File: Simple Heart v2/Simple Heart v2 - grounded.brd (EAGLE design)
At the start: 70 x 50 mm, 22 parts

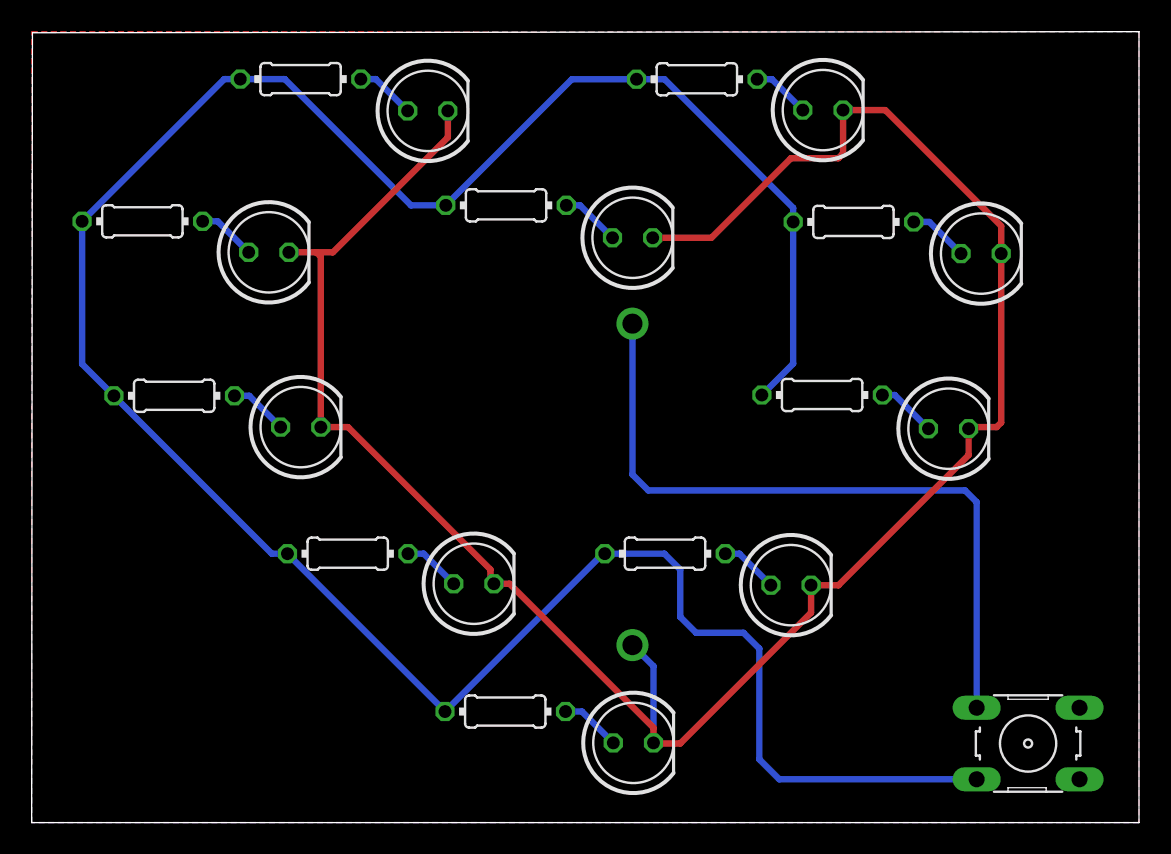
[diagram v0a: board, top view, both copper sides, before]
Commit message: Moving switch location a bit, added oshpark image. Need to confirm text.
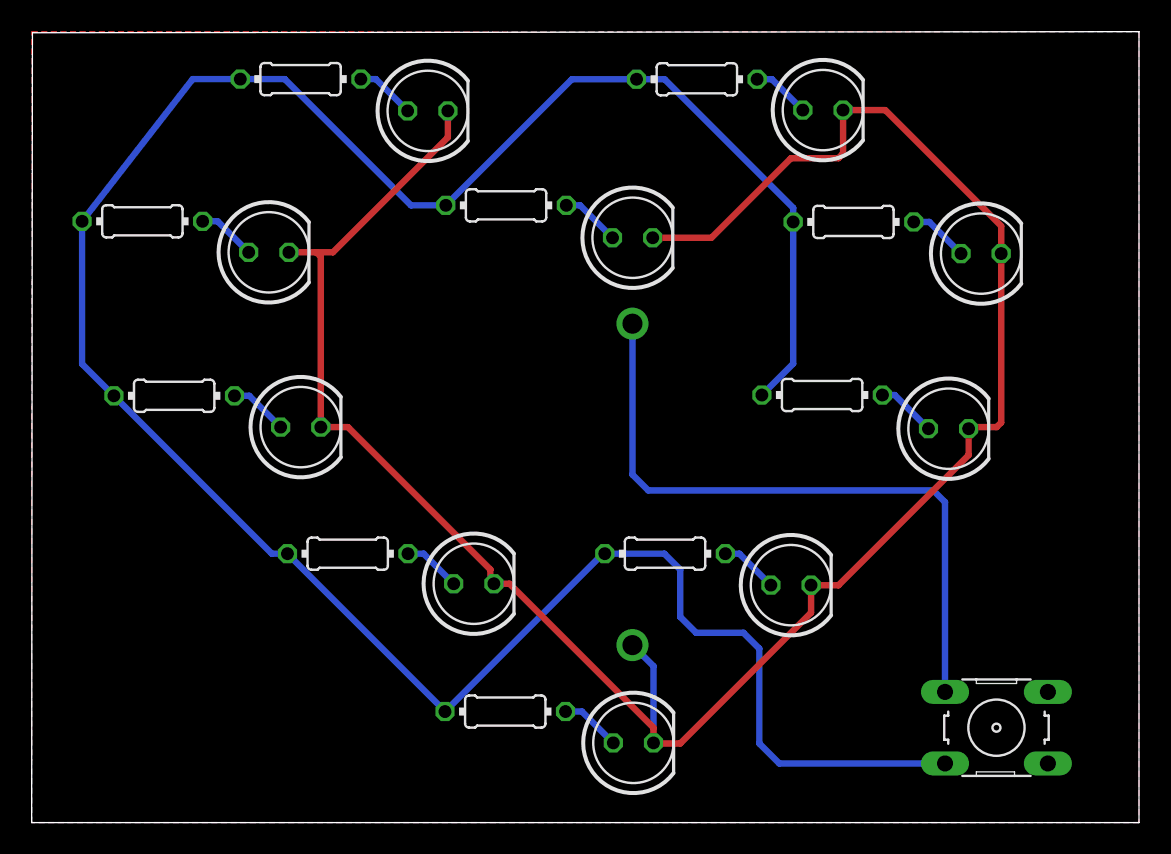
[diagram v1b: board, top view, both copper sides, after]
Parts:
- moved S1 2.24 mm to (61.0, 6.00)
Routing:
- net N$11: track 45.0 -> 42.0 mm
- net N$12: track 161.9 -> 159.6 mm
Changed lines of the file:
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@@
 <attribute name="VALUE" x="38.4144" y="16.5174" size="0.9906" layer="27" ratio="10"/>
 </element>
-<element name="S1" library="switch-omron" package="B3F-10XX" value="" x="62.99" y="5" smashed="yes">
-<attribute name="MPN" value="B3F-1000" x="62.99" y="5" size="1.778" layer="27" display="off"/>
-<attribute name="OC_NEWARK" value="36M3542" x="62.99" y="5" size="1.778" layer="27" display="off"/>
-<attribute name="OC_FARNELL" value="176432" x="62.99" y="5" size="1.778" layer="27" display="off"/>
-<attribute name="MF" value="" x="62.99" y="5" size="1.778" layer="27" display="off"/>
-<attribute name="NAME" x="62.942" y="9.683" size="1.27" layer="26" ratio="10" rot="MR0"/>
-<attribute name="VALUE" x="59.942" y="-0.08" size="1.27" layer="27" ratio="10"/>
+<element name="S1" library="switch-omron" package="B3F-10XX" value="" x="60.99" y="6" smashed="yes">
+<attribute name="MPN" value="B3F-1000" x="60.99" y="6" size="1.778" layer="27" display="off"/>
+<attribute name="OC_NEWARK" value="36M3542" x="60.99" y="6" size="1.778" layer="27" display="off"/>
+<attribute name="OC_FARNELL" value="176432" x="60.99" y="6" size="1.778" layer="27" display="off"/>
+<attribute name="MF" value="" x="60.99" y="6" size="1.778" layer="27" display="off"/>
+<attribute name="NAME" x="60.942" y="10.683" size="1.27" layer="26" ratio="10" rot="MR0"/>
+<attribute name="VALUE" x="57.942" y="0.92" size="1.27" layer="27" ratio="10"/>
 </element>
 </elements>
@@
 <wire x1="5.2" y1="26.98" x2="3.19" y2="28.99" width="0.4064" layer="16"/>
 <wire x1="3.19" y1="28.99" x2="3.19" y2="38.01" width="0.4064" layer="16"/>
-<wire x1="3.19" y1="38.01" x2="12.18" y2="47" width="0.4064" layer="16"/>
-<wire x1="12.18" y1="47" x2="13.19" y2="47" width="0.4064" layer="16"/>
+<wire x1="3.19" y1="38.01" x2="10.18" y2="47" width="0.4064" layer="16"/>
+<wire x1="10.18" y1="47" x2="13.19" y2="47" width="0.4064" layer="16"/>
 <wire x1="36.23" y1="17" x2="36.11" y2="17" width="0.4064" layer="16"/>
 <wire x1="36.11" y1="17" x2="26.13" y2="7.02" width="0.4064" layer="16"/>
@@
 <wire x1="40.01" y1="46.99" x2="48.14" y2="38.86" width="0.4064" layer="16"/>
 <wire x1="48.14" y1="37.97" x2="48.14" y2="38.86" width="0.4064" layer="16"/>
-<wire x1="59.7388" y1="2.7394" x2="47.2606" y2="2.7394" width="0.4064" layer="16"/>
-<wire x1="47.2606" y1="2.7394" x2="46" y2="4" width="0.4064" layer="16"/>
-<wire x1="46" y1="4" x2="46" y2="11" width="0.4064" layer="16"/>
+<wire x1="57.7388" y1="3.7394" x2="47.2606" y2="3.7394" width="0.4064" layer="16"/>
+<wire x1="47.2606" y1="3.7394" x2="46" y2="5" width="0.4064" layer="16"/>
+<wire x1="46" y1="5" x2="46" y2="11" width="0.4064" layer="16"/>
 <wire x1="46" y1="11" x2="45" y2="12" width="0.4064" layer="16"/>
 <wire x1="45" y1="12" x2="42" y2="12" width="0.4064" layer="16"/>
@@
 <contactref element="BATTERY_1" pad="+"/>
 <contactref element="S1" pad="1"/>
-<wire x1="59.7388" y1="7.2606" x2="59.7388" y2="20.2612" width="0.4064" layer="16"/>
+<wire x1="57.7388" y1="8.2606" x2="57.7388" y2="20.2612" width="0.4064" layer="16"/>
 <wire x1="37.98" y1="31.54" x2="37.98" y2="22" width="0.4064" layer="16"/>
-<wire x1="59.7388" y1="20.2612" x2="59" y2="21" width="0.4064" layer="16"/>
-<wire x1="59" y1="21" x2="38.98" y2="21" width="0.4064" layer="16"/>
+<wire x1="57.7388" y1="20.2612" x2="57" y2="21" width="0.4064" layer="16"/>
+<wire x1="57" y1="21" x2="38.98" y2="21" width="0.4064" layer="16"/>
 <wire x1="38.98" y1="21" x2="37.98" y2="22" width="0.4064" layer="16"/>
 </signal>

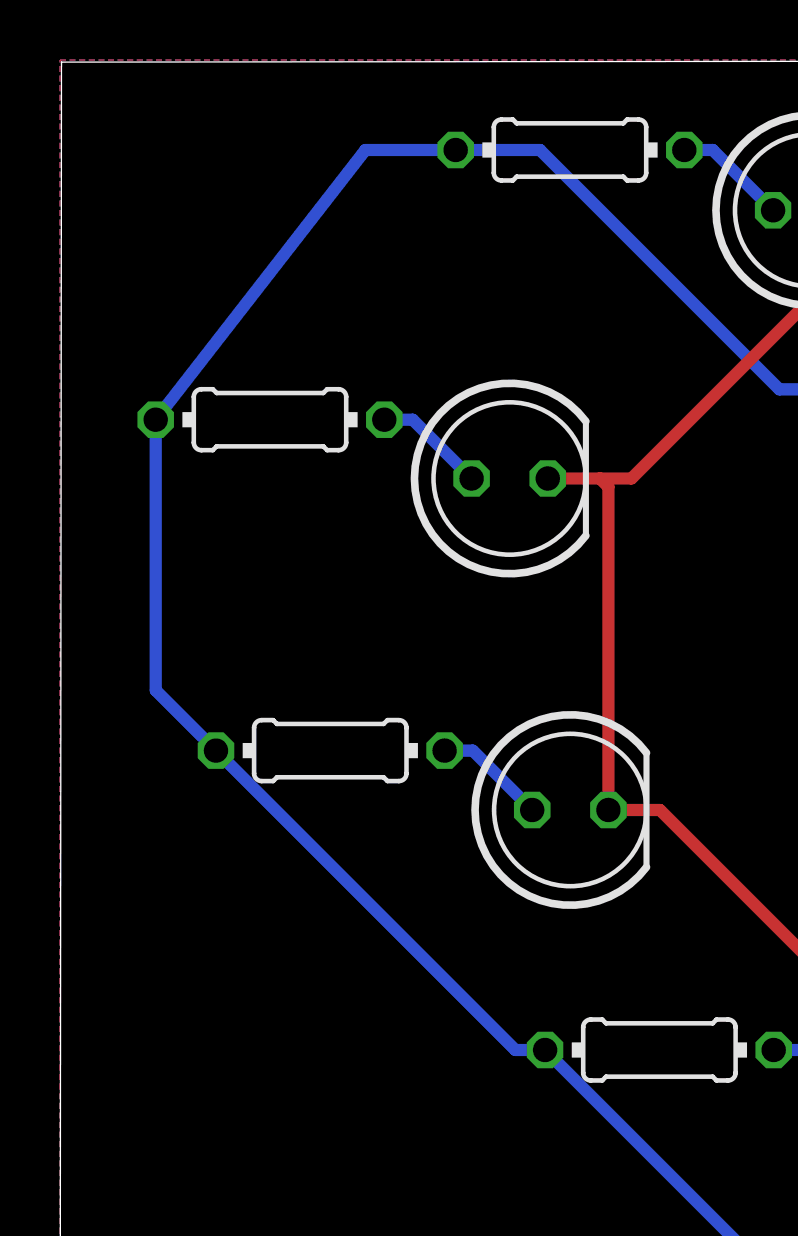
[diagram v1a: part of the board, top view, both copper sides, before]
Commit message: OCDing on the power line routing...it's not symetrical yet. But closer.
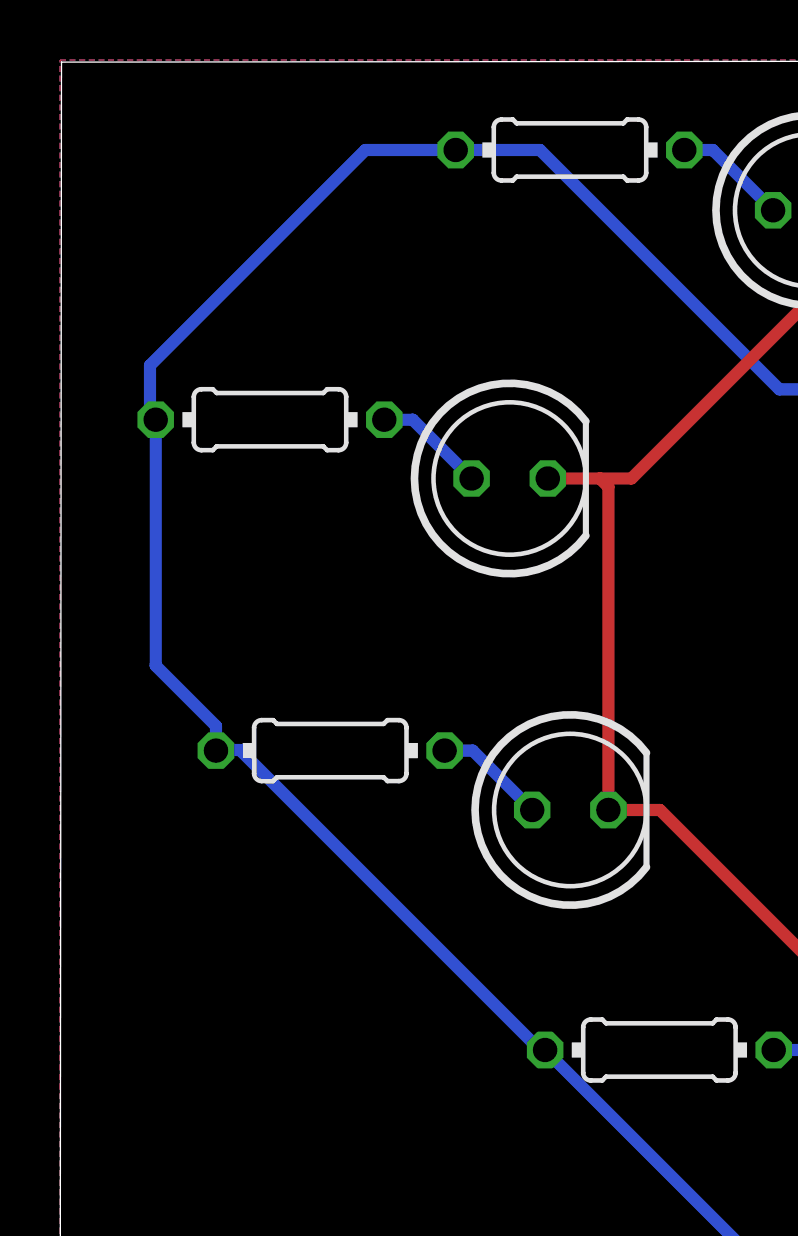
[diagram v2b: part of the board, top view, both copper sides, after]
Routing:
- net N$12: track 159.6 -> 160.2 mm
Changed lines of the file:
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@@
 <contactref element="R10" pad="1"/>
 <contactref element="S1" pad="3"/>
-<wire x1="26.13" y1="7.02" x2="26.13" y2="7.04" width="0.4064" layer="16"/>
-<wire x1="26.13" y1="7.04" x2="16.17" y2="17" width="0.4064" layer="16"/>
-<wire x1="16.17" y1="17" x2="15.18" y2="17" width="0.4064" layer="16"/>
-<wire x1="15.18" y1="17" x2="5.2" y2="26.98" width="0.4064" layer="16"/>
-<wire x1="5.2" y1="26.98" x2="3.19" y2="28.99" width="0.4064" layer="16"/>
-<wire x1="3.19" y1="28.99" x2="3.19" y2="38.01" width="0.4064" layer="16"/>
-<wire x1="3.19" y1="38.01" x2="10.18" y2="47" width="0.4064" layer="16"/>
 <wire x1="10.18" y1="47" x2="13.19" y2="47" width="0.4064" layer="16"/>
-<wire x1="36.23" y1="17" x2="36.11" y2="17" width="0.4064" layer="16"/>
-<wire x1="36.11" y1="17" x2="26.13" y2="7.02" width="0.4064" layer="16"/>
 <wire x1="46.16" y1="27.03" x2="48.14" y2="29.01" width="0.4064" layer="16"/>
 <wire x1="48.14" y1="29.01" x2="48.14" y2="37.97" width="0.4064" layer="16"/>
@@
 <wire x1="41" y1="16" x2="40" y2="17" width="0.4064" layer="16"/>
 <wire x1="40" y1="17" x2="36.23" y2="17" width="0.4064" layer="16"/>
+<wire x1="16.17" y1="17" x2="16" y2="17" width="0.4064" layer="16"/>
+<wire x1="16" y1="17" x2="6" y2="27" width="0.4064" layer="16"/>
+<wire x1="6" y1="27" x2="5.22" y2="27" width="0.4064" layer="16"/>
+<wire x1="5.22" y1="27" x2="5.2" y2="26.98" width="0.4064" layer="16"/>
+<wire x1="26.13" y1="7.02" x2="26.13" y2="7.04" width="0.4064" layer="16"/>
+<wire x1="26.13" y1="7.04" x2="16.17" y2="17" width="0.4064" layer="16"/>
+<wire x1="36.23" y1="17" x2="36.11" y2="17" width="0.4064" layer="16"/>
+<wire x1="36.11" y1="17" x2="26.13" y2="7.02" width="0.4064" layer="16"/>
+<wire x1="5.2" y1="26.98" x2="5.2" y2="27.8" width="0.4064" layer="16"/>
+<wire x1="5.2" y1="27.8" x2="3.19" y2="29.81" width="0.4064" layer="16"/>
+<wire x1="3.19" y1="29.81" x2="3.19" y2="38.01" width="0.4064" layer="16"/>
+<wire x1="10.18" y1="47" x2="3" y2="39.82" width="0.4064" layer="16"/>
+<wire x1="3.19" y1="38.01" x2="3" y2="38.2" width="0.4064" layer="16"/>
+<wire x1="3" y1="38.2" x2="3" y2="39.82" width="0.4064" layer="16"/>
 </signal>
 <signal name="N$11">
